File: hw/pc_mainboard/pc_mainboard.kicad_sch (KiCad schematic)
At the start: 0 parts

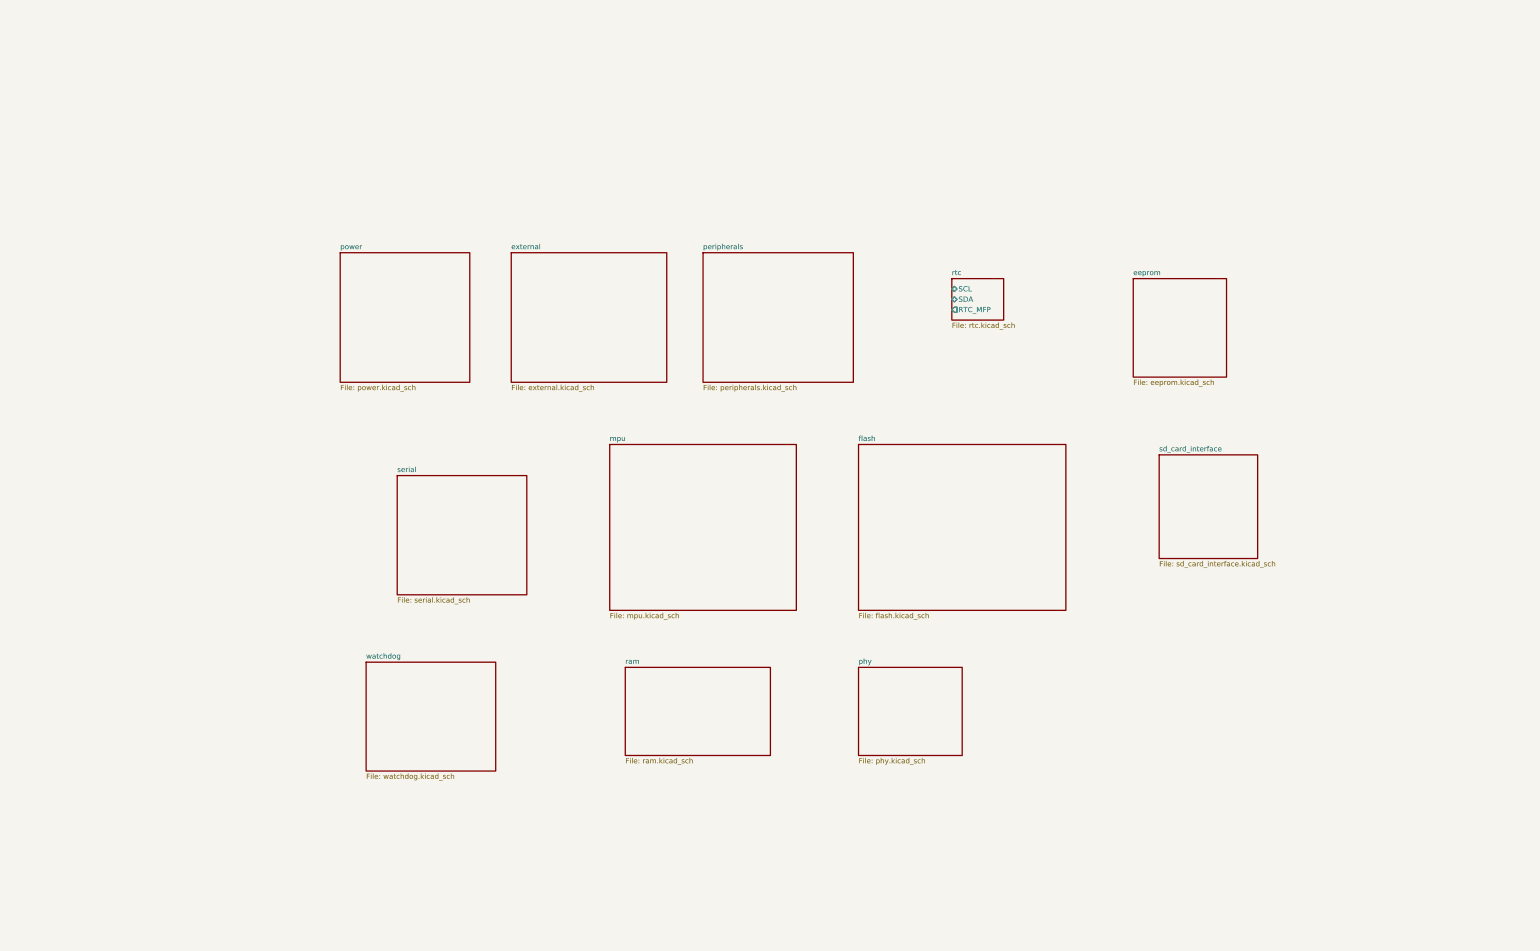
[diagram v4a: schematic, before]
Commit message: RAM Schematic Capture (#39)
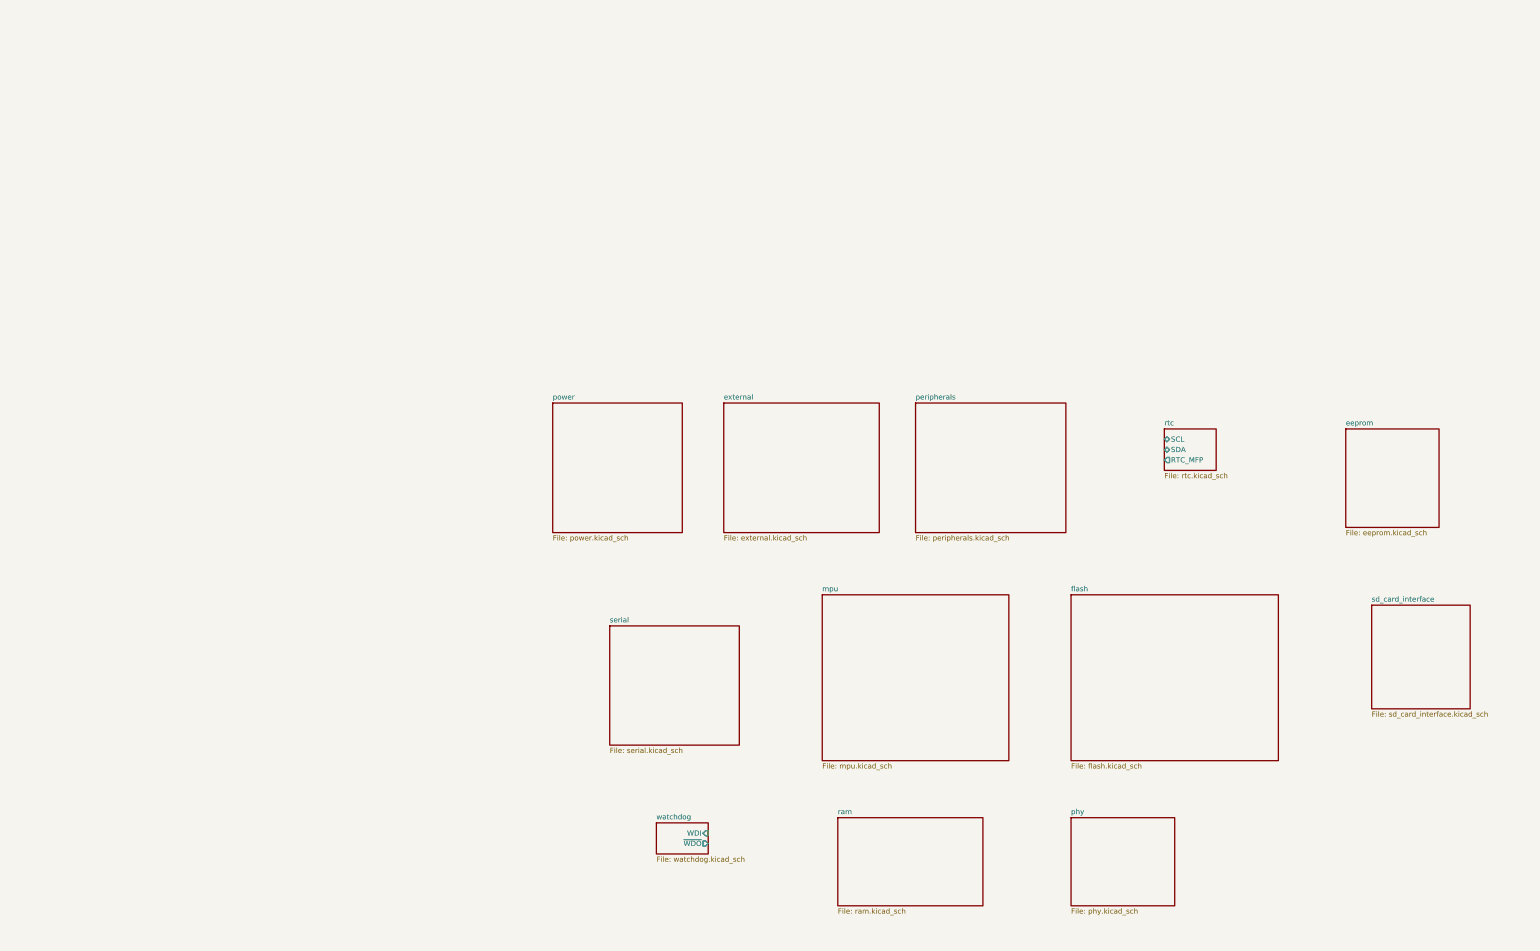
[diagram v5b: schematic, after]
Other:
- sheet watchdog ports: added WDI, ~{WDO}; removed none
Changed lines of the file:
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@@
 	(generator "eeschema")
 	(generator_version "8.0")
-	(paper "B")
+	(paper "A2")
 	(title_block
 		(title "Mainboard")
 	)
 	(sheet
-		(at 276.86 92.71)
+		(at 328.93 129.54)
 		(size 12.7 10.16)
 		(fields_autoplaced yes)
@@
 		)
 		(property "Sheetname" "rtc"
-			(at 276.86 91.9984 0)
+			(at 328.93 128.8284 0)
 			(effects
 				(font
@@
 		)
 		(property "Sheetfile" "rtc.kicad_sch"
-			(at 276.86 103.4546 0)
+			(at 328.93 140.2846 0)
 			(effects
 				(font
@@
 		)
 		(pin "RTC_MFP" output
-			(at 276.86 100.33 180)
+			(at 328.93 137.16 180)
 			(effects
 				(font
@@
 		)
 		(pin "SDA" bidirectional
-			(at 276.86 97.79 180)
+			(at 328.93 134.62 180)
 			(effects
 				(font
@@
 		)
 		(pin "SCL" bidirectional
-			(at 276.86 95.25 180)
+			(at 328.93 132.08 180)
 			(effects
 				(font
@@
 	)
 	(sheet
-		(at 321.31 92.71)
+		(at 373.38 129.54)
 		(size 22.86 24.13)
 		(fields_autoplaced yes)
@@
 		)
 		(property "Sheetname" "eeprom"
-			(at 321.31 91.9984 0)
+			(at 373.38 128.8284 0)
 			(effects
 				(font
@@
 		)
 		(property "Sheetfile" "eeprom.kicad_sch"
-			(at 321.31 117.4246 0)
+			(at 373.38 154.2546 0)
 			(effects
 				(font
@@
 	)
 	(sheet
-		(at 254 187.96)
+		(at 306.07 224.79)
 		(size 25.4 21.59)
 		(fields_autoplaced yes)
@@
 		)
 		(property "Sheetname" "phy"
-			(at 254 187.2484 0)
+			(at 306.07 224.0784 0)
 			(effects
 				(font
@@
 		)
 		(property "Sheetfile" "phy.kicad_sch"
-			(at 254 210.1346 0)
+			(at 306.07 246.9646 0)
 			(effects
 				(font
@@
 	)
 	(sheet
-		(at 327.66 135.89)
+		(at 379.73 172.72)
 		(size 24.13 25.4)
 		(fields_autoplaced yes)
@@
 		)
 		(property "Sheetname" "sd_card_interface"
-			(at 327.66 135.1784 0)
+			(at 379.73 172.0084 0)
 			(effects
 				(font
@@
 		)
 		(property "Sheetfile" "sd_card_interface.kicad_sch"
-			(at 327.66 161.8746 0)
+			(at 379.73 198.7046 0)
 			(effects
 				(font
@@
 	)
 	(sheet
-		(at 127 86.36)
+		(at 179.07 123.19)
 		(size 31.75 31.75)
 		(fields_autoplaced yes)
@@
 		)
 		(property "Sheetname" "power"
-			(at 127 85.6484 0)
+			(at 179.07 122.4784 0)
 			(effects
 				(font
@@
 		)
 		(property "Sheetfile" "power.kicad_sch"
-			(at 127 118.6946 0)
+			(at 179.07 155.5246 0)
 			(effects
 				(font
@@
 	)
 	(sheet
-		(at 215.9 86.36)
+		(at 267.97 123.19)
 		(size 36.83 31.75)
 		(fields_autoplaced yes)
@@
 		)
 		(property "Sheetname" "peripherals"
-			(at 215.9 85.6484 0)
+			(at 267.97 122.4784 0)
 			(effects
 				(font
@@
 		)
 		(property "Sheetfile" "peripherals.kicad_sch"
-			(at 215.9 118.6946 0)
+			(at 267.97 155.5246 0)
 			(effects
 				(font
@@
 	)
 	(sheet
-		(at 254 133.35)
+		(at 306.07 170.18)
 		(size 50.8 40.64)
 		(fields_autoplaced yes)
@@
 		)
 		(property "Sheetname" "flash"
-			(at 254 132.6384 0)
+			(at 306.07 169.4684 0)
 			(effects
 				(font
@@
 		)
 		(property "Sheetfile" "flash.kicad_sch"
-			(at 254 174.5746 0)
+			(at 306.07 211.4046 0)
 			(effects
 				(font
@@
 	)
 	(sheet
-		(at 133.35 186.69)
-		(size 31.75 26.67)
+		(at 204.47 226.06)
+		(size 12.7 7.62)
 		(fields_autoplaced yes)
 		(stroke
@@
 		)
 		(property "Sheetname" "watchdog"
-			(at 133.35 185.9784 0)
+			(at 204.47 225.3484 0)
 			(effects
 				(font
@@
 		)
 		(property "Sheetfile" "watchdog.kicad_sch"
-			(at 133.35 213.9446 0)
-			(effects
-				(font
-					(size 1.27 1.27)
-				)
-				(justify left top)
+			(at 204.47 234.2646 0)
+			(effects
+				(font
+					(size 1.27 1.27)
+				)
+				(justify left top)
+			)
+		)
+		(pin "WDI" input
+			(at 217.17 228.6 0)
+			(effects
+				(font
+					(size 1.27 1.27)
+				)
+				(justify right)
+			)
+		)
+		(pin "~{WDO}" output
+			(at 217.17 231.14 0)
+			(effects
+				(font
+					(size 1.27 1.27)
+				)
+				(justify right)
 			)
 		)
@@
 	)
 	(sheet
-		(at 193.04 133.35)
+		(at 245.11 170.18)
 		(size 45.72 40.64)
 		(fields_autoplaced yes)
@@
 		)
 		(property "Sheetname" "mpu"
-			(at 193.04 132.6384 0)
+			(at 245.11 169.4684 0)
 			(effects
 				(font
@@
 		)
 		(property "Sheetfile" "mpu.kicad_sch"
-			(at 193.04 174.5746 0)
+			(at 245.11 211.4046 0)
 			(effects
 				(font
@@
 	)
 	(sheet
-		(at 140.97 140.97)
+		(at 193.04 177.8)
 		(size 31.75 29.21)
 		(fields_autoplaced yes)
@@
 		)
 		(property "Sheetname" "serial"
-			(at 140.97 140.2584 0)
+			(at 193.04 177.0884 0)
 			(effects
 				(font
@@
 		)
 		(property "Sheetfile" "serial.kicad_sch"
-			(at 140.97 170.7646 0)
+			(at 193.04 207.5946 0)
 			(effects
 				(font
@@
 	)
 	(sheet
-		(at 168.91 86.36)
+		(at 220.98 123.19)
 		(size 38.1 31.75)
 		(fields_autoplaced yes)
@@
 		)
 		(property "Sheetname" "external"
-			(at 168.91 85.6484 0)
+			(at 220.98 122.4784 0)
 			(effects
 				(font
@@
 		)
 		(property "Sheetfile" "external.kicad_sch"
-			(at 168.91 118.6946 0)
+			(at 220.98 155.5246 0)
 			(effects
 				(font
@@
 	)
 	(sheet
-		(at 196.85 187.96)
+		(at 248.92 224.79)
 		(size 35.56 21.59)
 		(fields_autoplaced yes)
@@
 		)
 		(property "Sheetname" "ram"
-			(at 196.85 187.2484 0)
+			(at 248.92 224.0784 0)
 			(effects
 				(font
@@
 		)
 		(property "Sheetfile" "ram.kicad_sch"
-			(at 196.85 210.1346 0)
-			(effects
-				(font
+			(at 248.92 246.9646 0)
+			(effects
+				(font

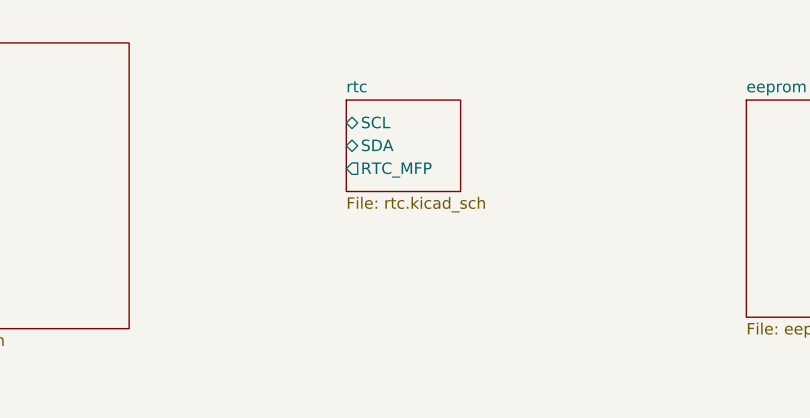
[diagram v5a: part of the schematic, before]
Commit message: eeprom schematic, partial layout
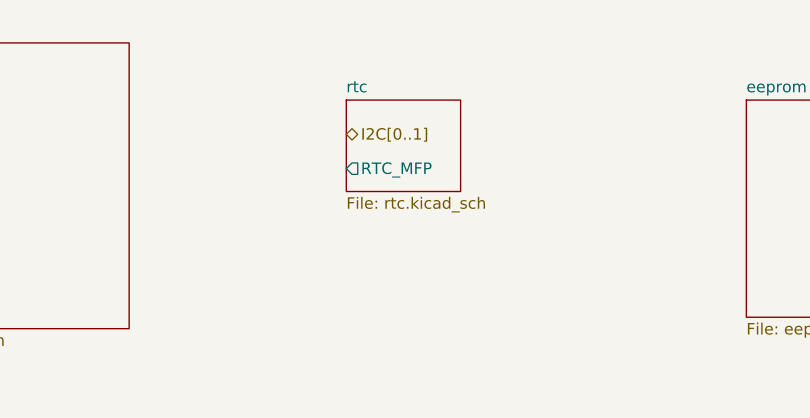
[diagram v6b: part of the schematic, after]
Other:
- sheet rtc ports: added none; removed SCL, SDA
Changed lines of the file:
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@@
 (kicad_sch
-	(version 20231120)
+	(version 20250114)
 	(generator "eeschema")
-	(generator_version "8.0")
+	(generator_version "9.0")
 	(paper "A2")
 	(title_block
 		(title "Mainboard")
 	)
+	(hierarchical_label "I2C[0..1]"
+		(shape bidirectional)
+		(at 328.93 133.35 0)
+		(effects
+			(font
+				(size 1.27 1.27)
+			)
+			(justify left)
+		)
+	)
 	(sheet
 		(at 328.93 129.54)
 		(size 12.7 10.16)
+		(exclude_from_sim no)
+		(in_bom yes)
+		(on_board yes)
+		(dnp no)
 		(fields_autoplaced yes)
 		(stroke
@@
 			)
 		)
-		(pin "SDA" bidirectional
-			(at 328.93 134.62 180)
-			(effects
-				(font
-					(size 1.27 1.27)
-				)
-				(justify left)
-			)
-		)
-		(pin "SCL" bidirectional
-			(at 328.93 132.08 180)
-			(effects
-				(font
-					(size 1.27 1.27)
-				)
-				(justify left)
-			)
-		)
 		(instances
 			(project "pc_mainboard"
@@
 		(at 373.38 129.54)
 		(size 22.86 24.13)
+		(exclude_from_sim no)
+		(in_bom yes)
+		(on_board yes)
+		(dnp no)
 		(fields_autoplaced yes)
 		(stroke
@@
 		(at 306.07 224.79)
 		(size 25.4 21.59)
+		(exclude_from_sim no)
+		(in_bom yes)
+		(on_board yes)
+		(dnp no)
 		(fields_autoplaced yes)
 		(stroke
@@
 		(at 379.73 172.72)
 		(size 24.13 25.4)
+		(exclude_from_sim no)
+		(in_bom yes)
+		(on_board yes)
+		(dnp no)
 		(fields_autoplaced yes)
 		(stroke
@@
 		(at 179.07 123.19)
 		(size 31.75 31.75)
+		(exclude_from_sim no)
+		(in_bom yes)
+		(on_board yes)
+		(dnp no)
 		(fields_autoplaced yes)
 		(stroke
@@
 		(at 267.97 123.19)
 		(size 36.83 31.75)
+		(exclude_from_sim no)
+		(in_bom yes)
+		(on_board yes)
+		(dnp no)
 		(fields_autoplaced yes)
 		(stroke
@@
 		(at 306.07 170.18)
 		(size 50.8 40.64)
+		(exclude_from_sim no)
+		(in_bom yes)
+		(on_board yes)
+		(dnp no)
 		(fields_autoplaced yes)
 		(stroke
@@
 		(at 204.47 226.06)
 		(size 12.7 7.62)
+		(exclude_from_sim no)
+		(in_bom yes)
+		(on_board yes)
+		(dnp no)
 		(fields_autoplaced yes)
 		(stroke
@@
 		(at 245.11 170.18)
 		(size 45.72 40.64)
+		(exclude_from_sim no)
+		(in_bom yes)
+		(on_board yes)
+		(dnp no)
 		(fields_autoplaced yes)
 		(stroke
@@
 		(at 193.04 177.8)
 		(size 31.75 29.21)
+		(exclude_from_sim no)
+		(in_bom yes)
+		(on_board yes)
+		(dnp no)
 		(fields_autoplaced yes)
 		(stroke
@@
 		(at 220.98 123.19)
 		(size 38.1 31.75)
+		(exclude_from_sim no)
+		(in_bom yes)
+		(on_board yes)
+		(dnp no)
 		(fields_autoplaced yes)
 		(stroke
@@
 		(at 248.92 224.79)
 		(size 35.56 21.59)
+		(exclude_from_sim no)
+		(in_bom yes)
+		(on_board yes)
+		(dnp no)
 		(fields_autoplaced yes)
 		(stroke
@@
 		)
 	)
+	(embedded_fonts no)
 )

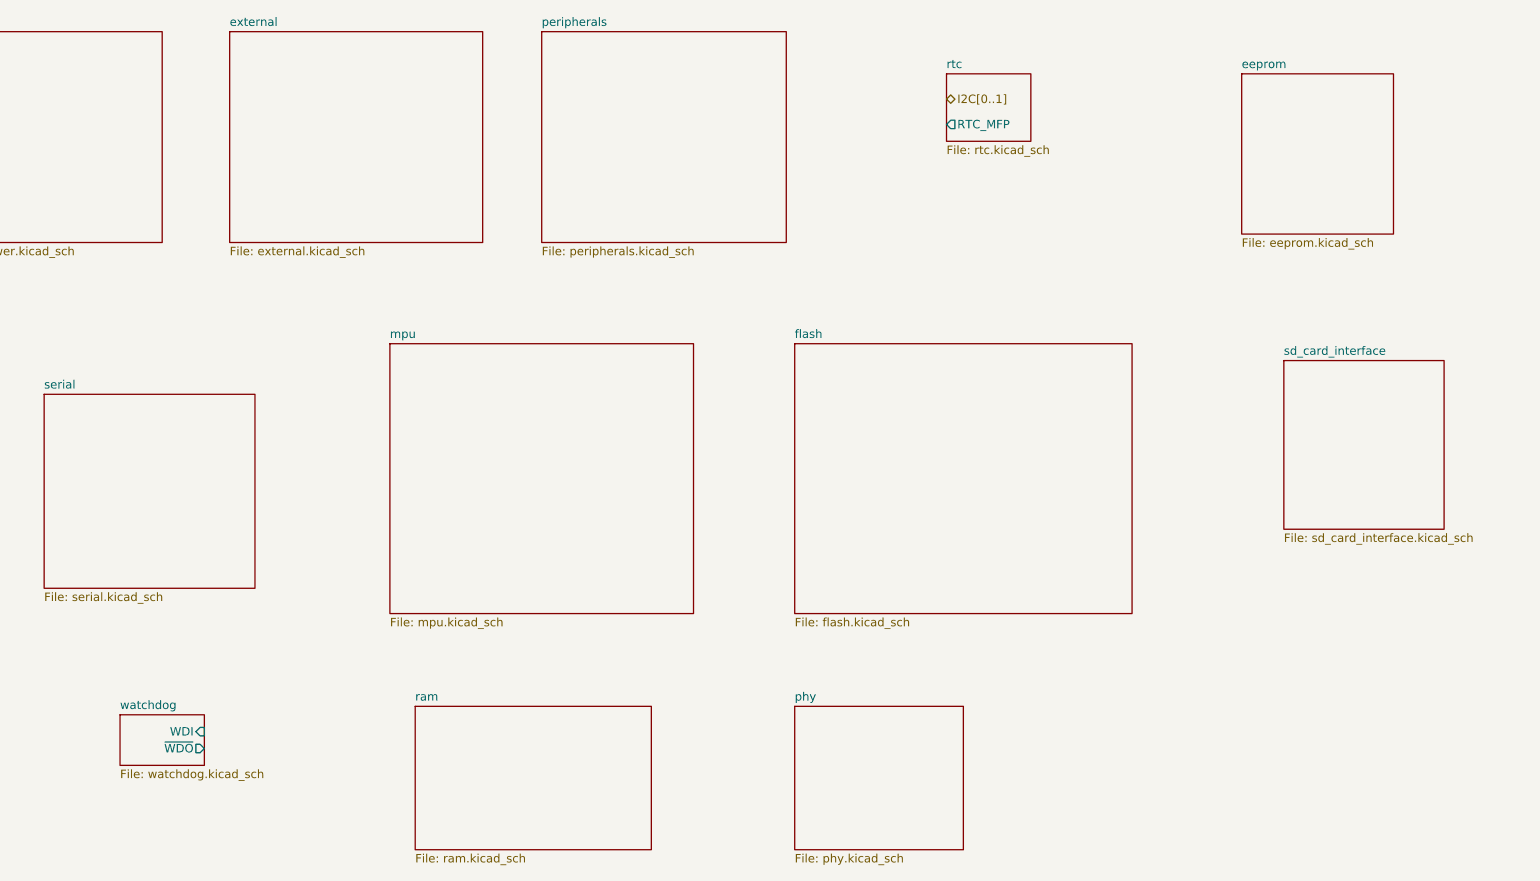
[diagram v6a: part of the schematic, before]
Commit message: Added I2C address table
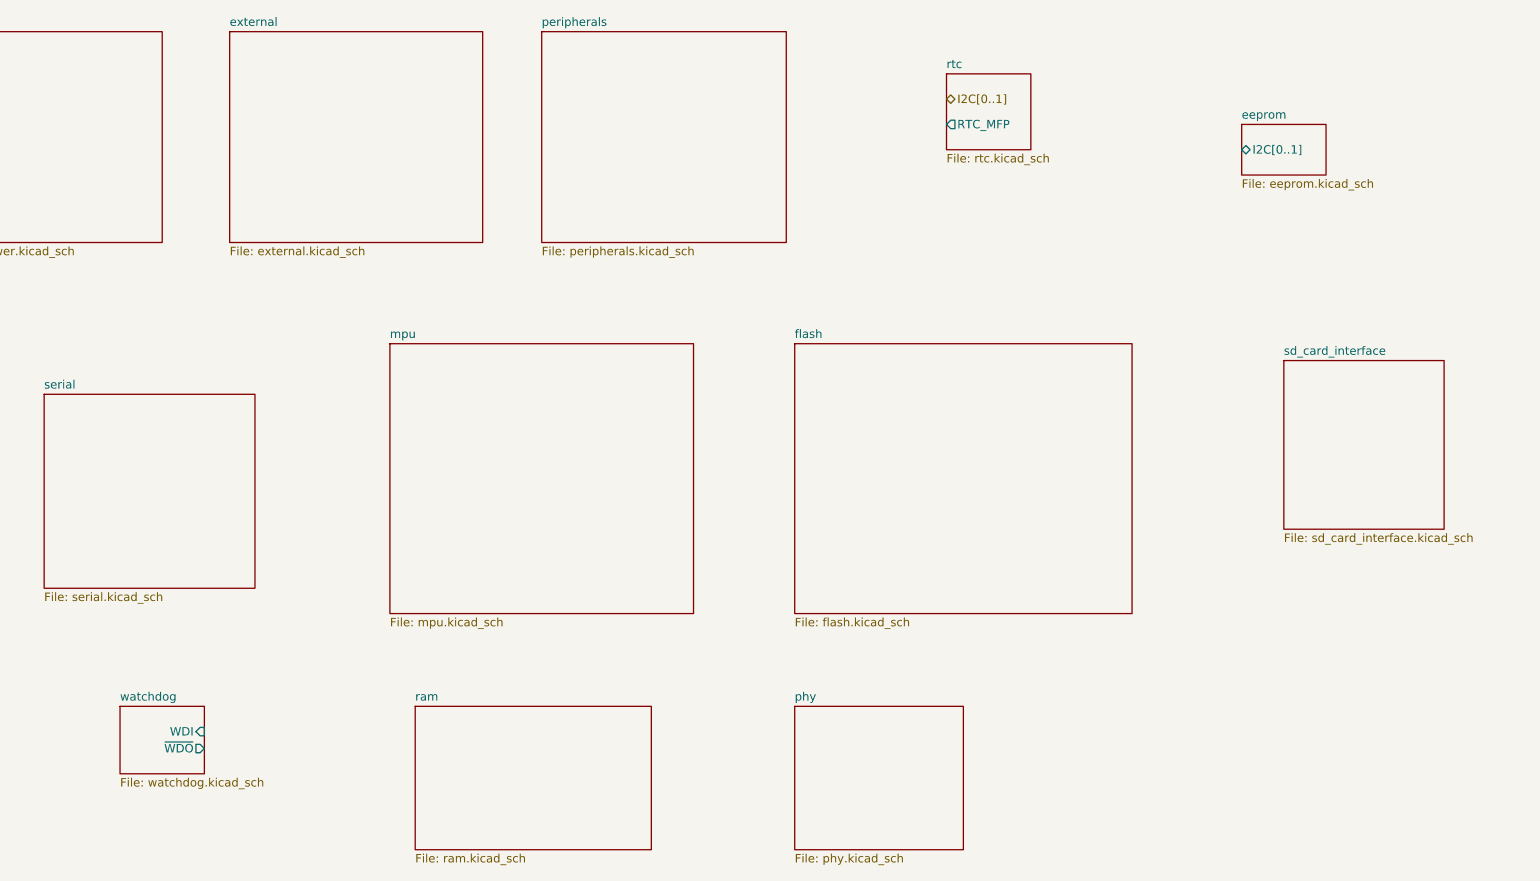
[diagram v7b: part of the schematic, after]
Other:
- sheet eeprom ports: added I2C[0..1]; removed none
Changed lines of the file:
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@@
 	(sheet
 		(at 328.93 129.54)
-		(size 12.7 10.16)
+		(size 12.7 11.43)
 		(exclude_from_sim no)
 		(in_bom yes)
@@
 		)
 		(property "Sheetfile" "rtc.kicad_sch"
-			(at 328.93 140.2846 0)
+			(at 328.93 141.5546 0)
 			(effects
 				(font
@@
 	)
 	(sheet
-		(at 373.38 129.54)
-		(size 22.86 24.13)
+		(at 373.38 137.16)
+		(size 12.7 7.62)
 		(exclude_from_sim no)
 		(in_bom yes)
@@
 		)
 		(property "Sheetname" "eeprom"
-			(at 373.38 128.8284 0)
+			(at 373.38 136.4484 0)
 			(effects
 				(font
@@
 		)
 		(property "Sheetfile" "eeprom.kicad_sch"
-			(at 373.38 154.2546 0)
-			(effects
-				(font
-					(size 1.27 1.27)
-				)
-				(justify left top)
+			(at 373.38 145.3646 0)
+			(effects
+				(font
+					(size 1.27 1.27)
+				)
+				(justify left top)
+			)
+		)
+		(pin "I2C[0..1]" bidirectional
+			(at 373.38 140.97 180)
+			(effects
+				(font
+					(size 1.27 1.27)
+				)
+				(justify left)
 			)
 		)
@@
 	)
 	(sheet
-		(at 204.47 226.06)
-		(size 12.7 7.62)
+		(at 204.47 224.79)
+		(size 12.7 10.16)
 		(exclude_from_sim no)
 		(in_bom yes)
@@
 		)
 		(property "Sheetname" "watchdog"
-			(at 204.47 225.3484 0)
+			(at 204.47 224.0784 0)
 			(effects
 				(font
@@
 		)
 		(property "Sheetfile" "watchdog.kicad_sch"
-			(at 204.47 234.2646 0)
-			(effects
-				(font
+			(at 204.47 235.5346 0)
+			(effects
+				(font
